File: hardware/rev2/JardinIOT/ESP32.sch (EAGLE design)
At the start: 5 parts, among them IC1 7815TV

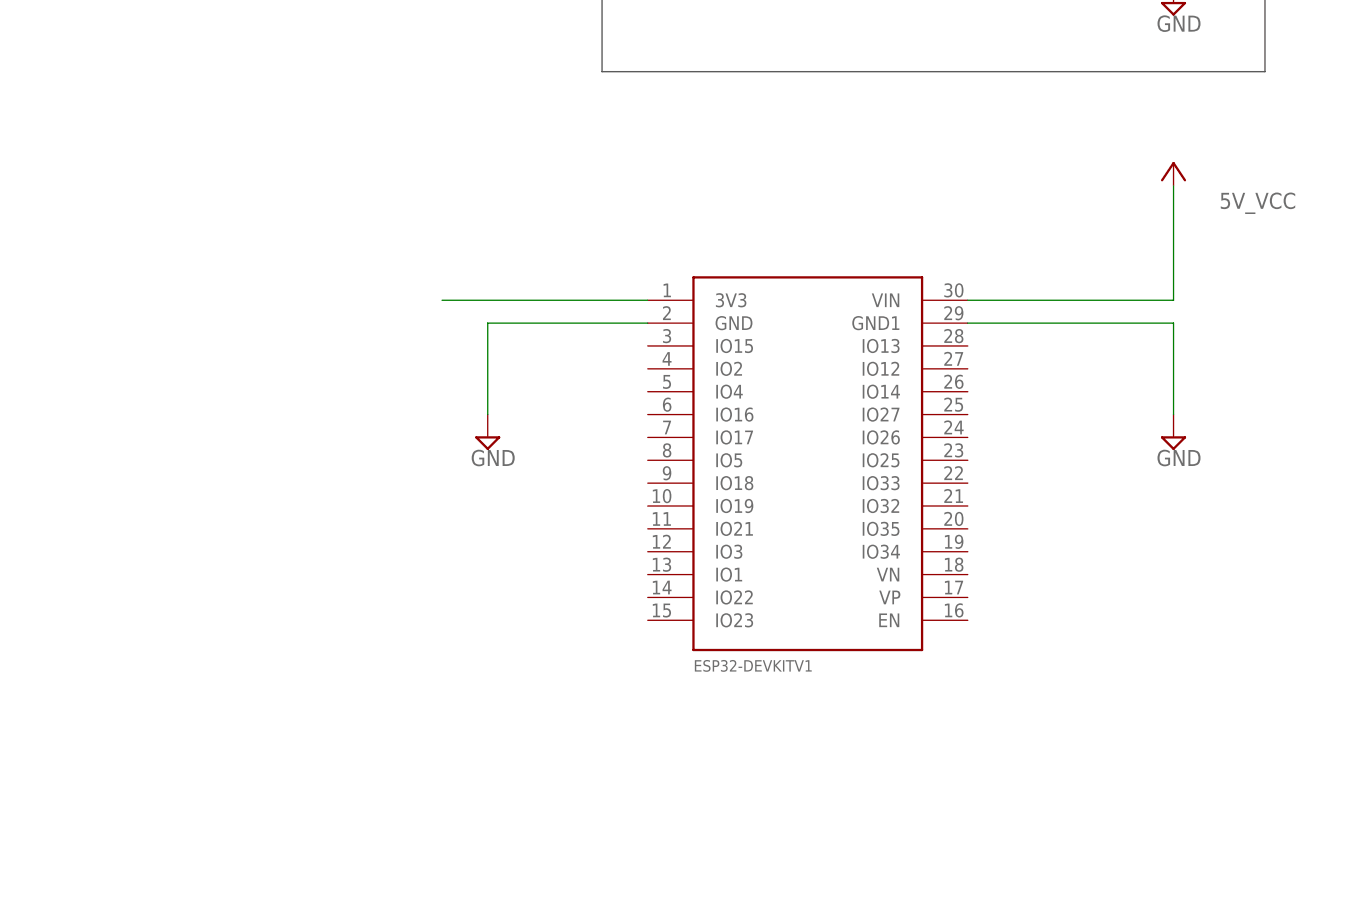
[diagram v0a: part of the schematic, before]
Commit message: Ajout de bouton multi-utilitaires sur la plaquette.
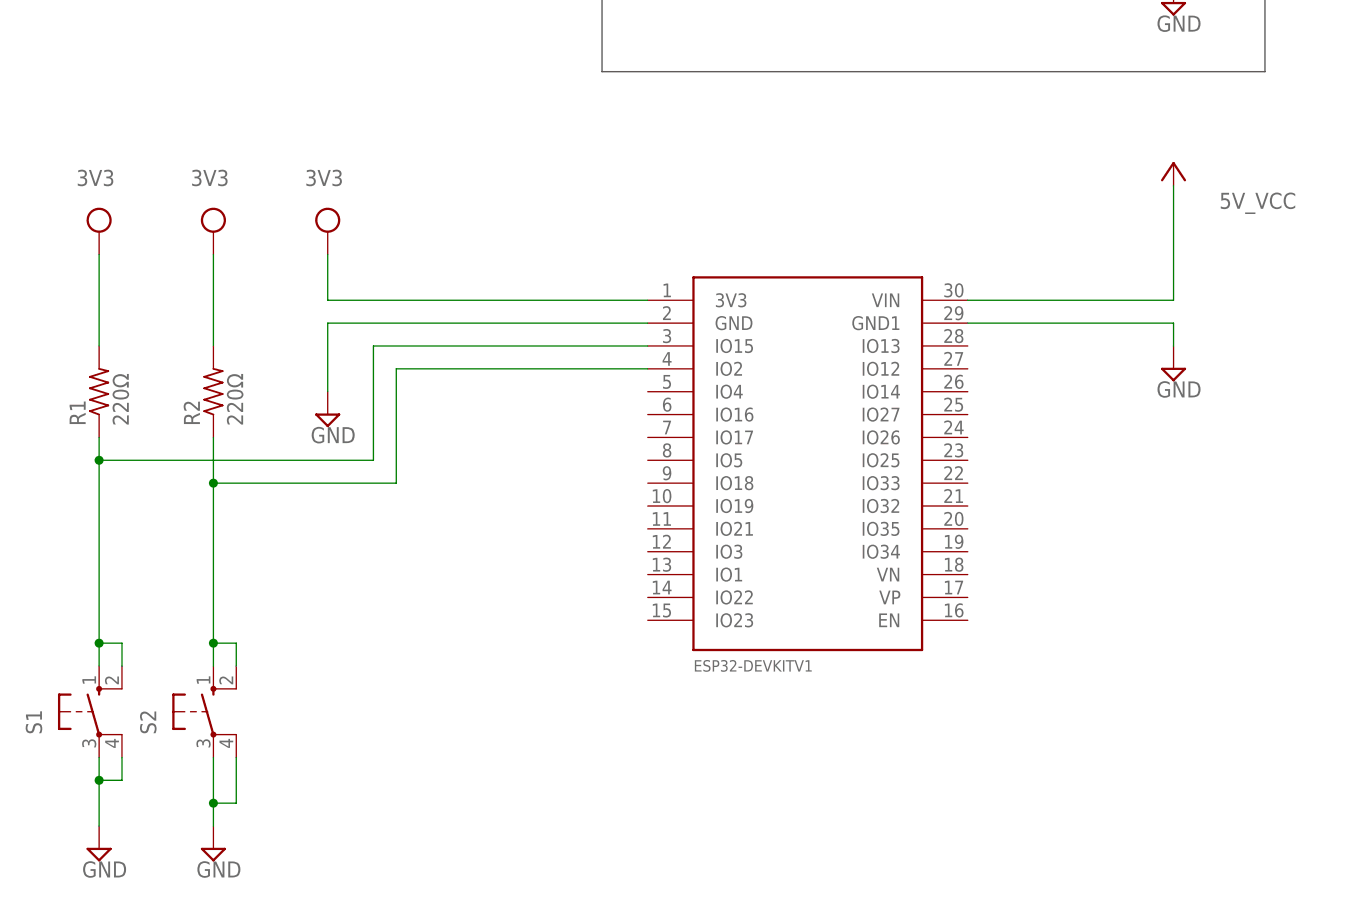
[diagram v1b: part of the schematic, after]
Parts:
- added R1, R2: 220Ω, rcl:R-US_0204/5
- added S1, S2: (no value), switch-omron:10-XX
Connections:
- removed net N$2: U$1.3V3
- new net 3V3: R1.2, R2.2, U$1.3V3
- new net N$1: R1.1, S1.S, S1.S1, U$1.IO15
- new net N$3: R2.1, S2.S, S2.S1, U$1.IO2
- net GND: now also S1.P, S1.P1, S2.P, S2.P1
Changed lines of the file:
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@@
 <part name="X1" library="con-wago-500" library_urn="urn:adsk.eagle:library:195" deviceset="W237-113" device="" package3d_urn="urn:adsk.eagle:package:10690/1"/>
 <part name="SUPPLY4" library="supply2" library_urn="urn:adsk.eagle:library:372" deviceset="GND" device=""/>
+<part name="R1" library="rcl" library_urn="urn:adsk.eagle:library:334" deviceset="R-US_" device="0204/5" package3d_urn="urn:adsk.eagle:package:23488/1" value="220Ω"/>
+<part name="R2" library="rcl" library_urn="urn:adsk.eagle:library:334" deviceset="R-US_" device="0204/5" package3d_urn="urn:adsk.eagle:package:23488/1" value="220Ω"/>
+<part name="S1" library="switch-omron" library_urn="urn:adsk.eagle:library:377" deviceset="10-XX" device="" package3d_urn="urn:adsk.eagle:package:27496/1"/>
+<part name="S2" library="switch-omron" library_urn="urn:adsk.eagle:library:377" deviceset="10-XX" device="" package3d_urn="urn:adsk.eagle:package:27496/1"/>
+<part name="SUPPLY5" library="supply2" library_urn="urn:adsk.eagle:library:372" deviceset="GND" device=""/>
+<part name="SUPPLY6" library="supply2" library_urn="urn:adsk.eagle:library:372" deviceset="GND" device=""/>
+<part name="SUPPLY7" library="supply2" library_urn="urn:adsk.eagle:library:372" deviceset="VCC" device=""/>
+<part name="SUPPLY8" library="supply2" library_urn="urn:adsk.eagle:library:372" deviceset="VCC" device=""/>
+<part name="SUPPLY9" library="supply2" library_urn="urn:adsk.eagle:library:372" deviceset="VCC" device=""/>
 </parts>
 <sheets>
@@
 <instance part="P+1" gate="VCC" x="-48.26" y="215.9" smashed="yes"/>
 <instance part="P+2" gate="VCC" x="-48.26" y="149.86" smashed="yes"/>
-<instance part="SUPPLY2" gate="GND" x="-48.26" y="119.38" smashed="yes">
-<attribute name="VALUE" x="-50.165" y="116.205" size="1.778" layer="96"/>
+<instance part="SUPPLY2" gate="GND" x="-48.26" y="127" smashed="yes">
+<attribute name="VALUE" x="-50.165" y="123.825" size="1.778" layer="96"/>
 </instance>
 <instance part="X1" gate="-1" x="-104.14" y="198.12" smashed="yes">
@@
 <attribute name="NAME" x="-104.14" y="181.229" size="1.778" layer="95" rot="R180"/>
 </instance>
-<instance part="SUPPLY4" gate="GND" x="-124.46" y="119.38" smashed="yes">
-<attribute name="VALUE" x="-126.365" y="116.205" size="1.778" layer="96"/>
-</instance>
+<instance part="SUPPLY4" gate="GND" x="-142.24" y="121.92" smashed="yes">
+<attribute name="VALUE" x="-144.145" y="118.745" size="1.778" layer="96"/>
+</instance>
+<instance part="R1" gate="G$1" x="-167.64" y="124.46" smashed="yes" rot="R90">
+<attribute name="NAME" x="-169.1386" y="120.65" size="1.778" layer="95" rot="R90"/>
+<attribute name="VALUE" x="-164.338" y="120.65" size="1.778" layer="96" rot="R90"/>
+</instance>
+<instance part="R2" gate="G$1" x="-154.94" y="124.46" smashed="yes" rot="R90">
+<attribute name="NAME" x="-156.4386" y="120.65" size="1.778" layer="95" rot="R90"/>
+<attribute name="VALUE" x="-151.638" y="120.65" size="1.778" layer="96" rot="R90"/>
+</instance>
+<instance part="S1" gate="1" x="-167.64" y="88.9" smashed="yes">
+<attribute name="NAME" x="-173.99" y="86.36" size="1.778" layer="95" rot="R90"/>
+<attribute name="VALUE" x="-171.45" y="92.075" size="1.778" layer="96" rot="R90"/>
+</instance>
+<instance part="S2" gate="1" x="-154.94" y="88.9" smashed="yes">
+<attribute name="NAME" x="-161.29" y="86.36" size="1.778" layer="95" rot="R90"/>
+<attribute name="VALUE" x="-158.75" y="92.075" size="1.778" layer="96" rot="R90"/>
+</instance>
+<instance part="SUPPLY5" gate="GND" x="-167.64" y="73.66" smashed="yes">
+<attribute name="VALUE" x="-169.545" y="70.485" size="1.778" layer="96"/>
+</instance>
+<instance part="SUPPLY6" gate="GND" x="-154.94" y="73.66" smashed="yes">
+<attribute name="VALUE" x="-156.845" y="70.485" size="1.778" layer="96"/>
+</instance>
+<instance part="SUPPLY7" gate="G$1" x="-142.24" y="142.24" smashed="yes"/>
+<instance part="SUPPLY8" gate="G$1" x="-154.94" y="142.24" smashed="yes"/>
+<instance part="SUPPLY9" gate="G$1" x="-167.64" y="142.24" smashed="yes"/>
 </instances>
 <busses>
@@
 <segment>
 <pinref part="SUPPLY2" gate="GND" pin="GND"/>
-<wire x1="-48.26" y1="132.08" x2="-48.26" y2="121.92" width="0.1524" layer="91"/>
+<wire x1="-48.26" y1="132.08" x2="-48.26" y2="129.54" width="0.1524" layer="91"/>
 <pinref part="U$1" gate="G$1" pin="GND1"/>
 <wire x1="-48.26" y1="132.08" x2="-71.12" y2="132.08" width="0.1524" layer="91"/>
@@
 <segment>
 <pinref part="U$1" gate="G$1" pin="GND"/>
-<wire x1="-106.68" y1="132.08" x2="-124.46" y2="132.08" width="0.1524" layer="91"/>
+<wire x1="-106.68" y1="132.08" x2="-142.24" y2="132.08" width="0.1524" layer="91"/>
 <pinref part="SUPPLY4" gate="GND" pin="GND"/>
-<wire x1="-124.46" y1="132.08" x2="-124.46" y2="121.92" width="0.1524" layer="91"/>
-</segment>
-</net>
-<net name="N$2" class="0">
-<segment>
-<pinref part="U$1" gate="G$1" pin="3V3"/>
-<wire x1="-106.68" y1="134.62" x2="-129.54" y2="134.62" width="0.1524" layer="91"/>
+<wire x1="-142.24" y1="132.08" x2="-142.24" y2="124.46" width="0.1524" layer="91"/>
+</segment>
+<segment>
+<pinref part="SUPPLY5" gate="GND" pin="GND"/>
+<pinref part="S1" gate="1" pin="P"/>
+<wire x1="-167.64" y1="83.82" x2="-167.64" y2="81.28" width="0.1524" layer="91"/>
+<pinref part="S1" gate="1" pin="P1"/>
+<wire x1="-167.64" y1="81.28" x2="-167.64" y2="76.2" width="0.1524" layer="91"/>
+<wire x1="-165.1" y1="83.82" x2="-165.1" y2="81.28" width="0.1524" layer="91"/>
+<wire x1="-165.1" y1="81.28" x2="-167.64" y2="81.28" width="0.1524" layer="91"/>
+<junction x="-167.64" y="81.28"/>
+</segment>
+<segment>
+<pinref part="SUPPLY6" gate="GND" pin="GND"/>
+<wire x1="-154.94" y1="78.74" x2="-154.94" y2="76.2" width="0.1524" layer="91"/>
+<pinref part="S2" gate="1" pin="P1"/>
+<wire x1="-152.4" y1="83.82" x2="-152.4" y2="78.74" width="0.1524" layer="91"/>
+<wire x1="-152.4" y1="78.74" x2="-154.94" y2="78.74" width="0.1524" layer="91"/>
+<pinref part="S2" gate="1" pin="P"/>
+<wire x1="-154.94" y1="83.82" x2="-154.94" y2="78.74" width="0.1524" layer="91"/>
+<junction x="-154.94" y="78.74"/>
 </segment>
 </net>
@@
 </segment>
 </net>
+<net name="N$1" class="0">
+<segment>
+<pinref part="R1" gate="G$1" pin="1"/>
+<wire x1="-167.64" y1="119.38" x2="-167.64" y2="116.84" width="0.1524" layer="91"/>
+<wire x1="-167.64" y1="116.84" x2="-167.64" y2="96.52" width="0.1524" layer="91"/>
+<wire x1="-167.64" y1="96.52" x2="-165.1" y2="96.52" width="0.1524" layer="91"/>
+<pinref part="S1" gate="1" pin="S1"/>
+<wire x1="-165.1" y1="96.52" x2="-165.1" y2="93.98" width="0.1524" layer="91"/>
+<pinref part="S1" gate="1" pin="S"/>
+<wire x1="-167.64" y1="96.52" x2="-167.64" y2="93.98" width="0.1524" layer="91"/>
+<junction x="-167.64" y="96.52"/>
+<pinref part="U$1" gate="G$1" pin="IO15"/>
+<wire x1="-106.68" y1="129.54" x2="-137.16" y2="129.54" width="0.1524" layer="91"/>
+<wire x1="-137.16" y1="129.54" x2="-137.16" y2="116.84" width="0.1524" layer="91"/>
+<wire x1="-137.16" y1="116.84" x2="-167.64" y2="116.84" width="0.1524" layer="91"/>
+<junction x="-167.64" y="116.84"/>
+</segment>
+</net>
+<net name="N$3" class="0">
+<segment>
+<pinref part="R2" gate="G$1" pin="1"/>
+<pinref part="S2" gate="1" pin="S"/>
+<wire x1="-154.94" y1="119.38" x2="-154.94" y2="114.3" width="0.1524" layer="91"/>
+<wire x1="-154.94" y1="114.3" x2="-154.94" y2="96.52" width="0.1524" layer="91"/>
+<wire x1="-154.94" y1="96.52" x2="-154.94" y2="93.98" width="0.1524" layer="91"/>
+<wire x1="-154.94" y1="96.52" x2="-152.4" y2="96.52" width="0.1524" layer="91"/>
+<junction x="-154.94" y="96.52"/>
+<pinref part="S2" gate="1" pin="S1"/>
+<wire x1="-152.4" y1="96.52" x2="-152.4" y2="93.98" width="0.1524" layer="91"/>
+<wire x1="-154.94" y1="114.3" x2="-134.62" y2="114.3" width="0.1524" layer="91"/>
+<wire x1="-134.62" y1="114.3" x2="-134.62" y2="127" width="0.1524" layer="91"/>
+<junction x="-154.94" y="114.3"/>
+<pinref part="U$1" gate="G$1" pin="IO2"/>
+<wire x1="-134.62" y1="127" x2="-106.68" y2="127" width="0.1524" layer="91"/>
+</segment>
+</net>
+<net name="3V3" class="0">
+<segment>
+<pinref part="U$1" gate="G$1" pin="3V3"/>
+<pinref part="SUPPLY7" gate="G$1" pin="VCC"/>
+<wire x1="-106.68" y1="134.62" x2="-142.24" y2="134.62" width="0.1524" layer="91"/>
+<wire x1="-142.24" y1="134.62" x2="-142.24" y2="139.7" width="0.1524" layer="91"/>
+<label x="-144.78" y="147.32" size="1.778" layer="95"/>
+</segment>
+<segment>
+<pinref part="SUPPLY8" gate="G$1" pin="VCC"/>
+<label x="-157.48" y="147.32" size="1.778" layer="95"/>
+<pinref part="R2" gate="G$1" pin="2"/>
+<wire x1="-154.94" y1="129.54" x2="-154.94" y2="139.7" width="0.1524" layer="91"/>
+</segment>
+<segment>
+<pinref part="SUPPLY9" gate="G$1" pin="VCC"/>
+<label x="-170.18" y="147.32" size="1.778" layer="95"/>
+<pinref part="R1" gate="G$1" pin="2"/>
+<wire x1="-167.64" y1="139.7" x2="-167.64" y2="129.54" width="0.1524" layer="91"/>
+</segment>
+</net>
